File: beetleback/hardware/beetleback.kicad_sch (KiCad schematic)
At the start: 24 parts, among them J1 Conn_01x05_Female, J3 motor_pad_1, J4 motor_pad_2, Q1 IRF7351TRPBF, Q2 IRF7351TRPBF, U1 ATtiny13A-SS, U2 DRV8701P

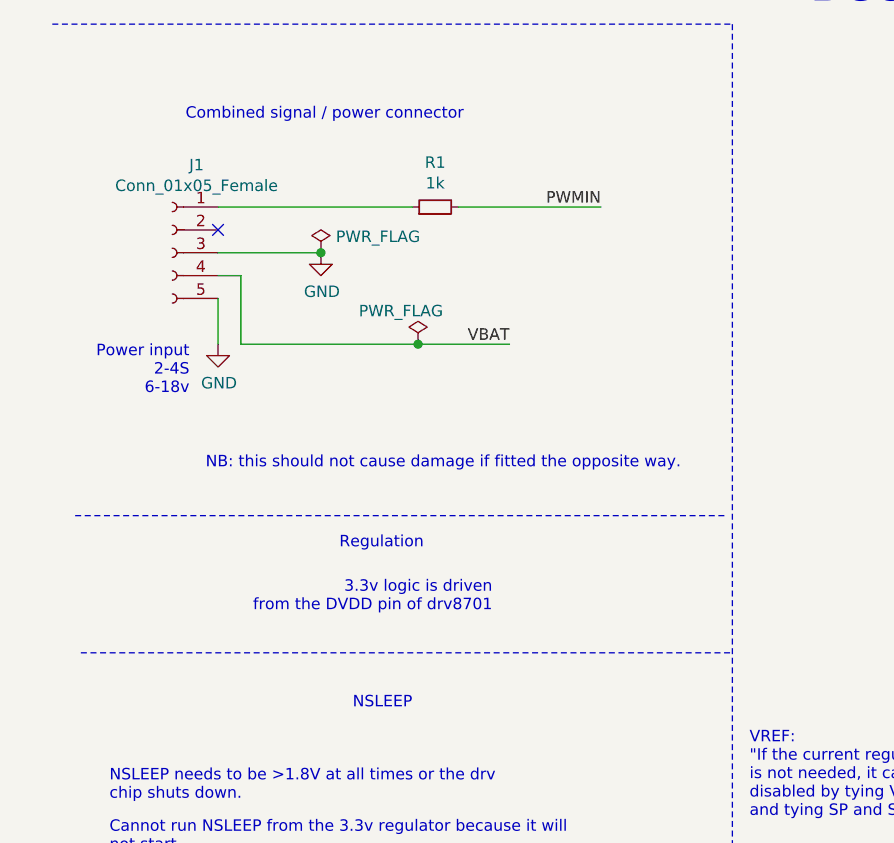
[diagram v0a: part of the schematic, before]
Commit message: Optional 5v regulator for RX
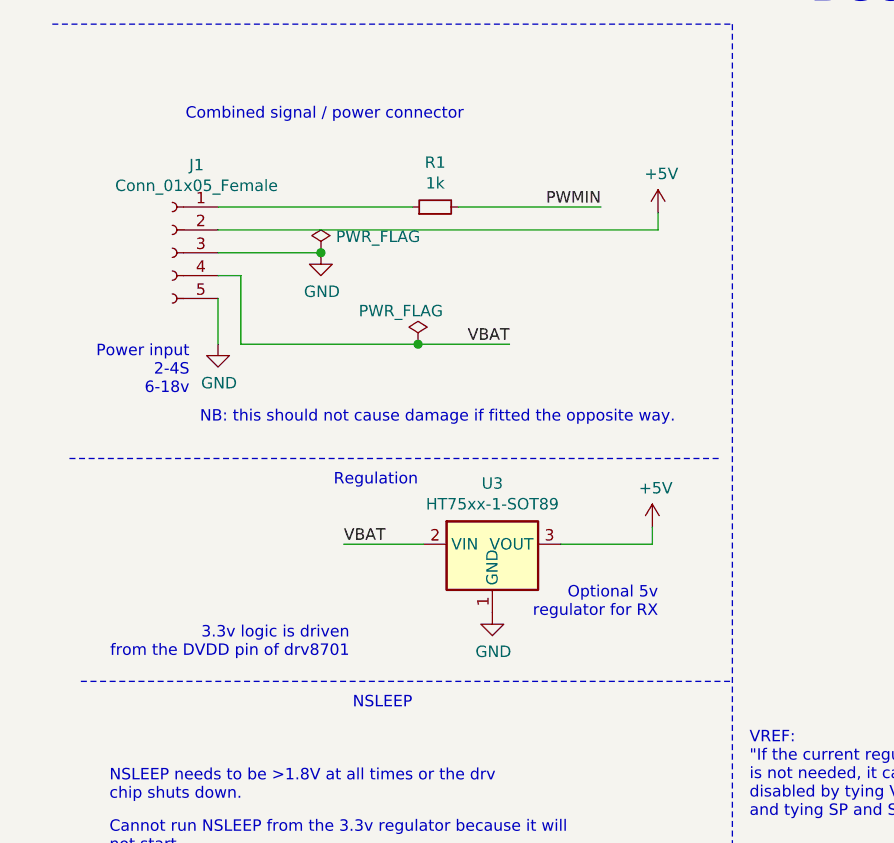
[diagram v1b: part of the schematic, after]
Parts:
- added U3: HT75xx-1-SOT89, Package_TO_SOT_SMD:SOT-89-3, symbol Regulator_Linear:HT75xx-1-SOT89
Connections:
- net GND: now also U3.1 (GND)
- net VBAT: now also U3.2 (VIN)
- net +5V: now reaches J1.2 (Pin_2)
- net +5V: now also U3.3 (VOUT)
- no-connect marks 4 -> 3
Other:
- note added: "Optional 5v regulator for RX"
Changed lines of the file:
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@@
   (junction (at 244.475 135.89) (diameter 1.016) (color 0 0 0 0))
   (junction (at 244.475 137.16) (diameter 1.016) (color 0 0 0 0))
-  (no_connect (at 27.94 50.8))
   (no_connect (at 178.435 66.04))
   (no_connect (at 182.88 118.745))
@@
     (stroke (width 0) (type solid) (color 0 0 0 0))
   )
+  (wire (pts (xy 27.94 50.8) (xy 76.835 50.8))
+    (stroke (width 0) (type solid) (color 0 0 0 0))
+  )
   (wire (pts (xy 27.94 53.34) (xy 39.37 53.34))
     (stroke (width 0) (type solid) (color 0 0 0 0))
@@
     (stroke (width 0) (type solid) (color 0 0 0 0))
   )
+  (wire (pts (xy 41.91 85.725) (xy 50.8 85.725))
+    (stroke (width 0) (type solid) (color 0 0 0 0))
+  )
   (wire (pts (xy 44.45 125.095) (xy 44.45 125.73))
     (stroke (width 0) (type solid) (color 0 0 0 0))
@@
     (stroke (width 0) (type solid) (color 0 0 0 0))
   )
+  (wire (pts (xy 66.04 85.725) (xy 76.2 85.725))
+    (stroke (width 0) (type solid) (color 0 0 0 0))
+  )
   (wire (pts (xy 67.945 170.18) (xy 76.835 170.18))
     (stroke (width 0) (type solid) (color 0 0 0 0))
@@
   )
   (wire (pts (xy 67.945 179.07) (xy 77.47 179.07))
+    (stroke (width 0) (type solid) (color 0 0 0 0))
+  )
+  (wire (pts (xy 76.2 83.82) (xy 76.2 85.725))
+    (stroke (width 0) (type solid) (color 0 0 0 0))
+  )
+  (wire (pts (xy 76.835 50.8) (xy 76.835 48.895))
     (stroke (width 0) (type solid) (color 0 0 0 0))
   )
@@
     (stroke (width 0) (type dash) (color 0 0 0 0))
   )
-  (polyline (pts (xy 12.065 82.55) (xy 84.455 82.55))
+  (polyline (pts (xy 11.43 76.2) (xy 83.82 76.2))
     (stroke (width 0) (type dash) (color 0 0 0 0))
   )
@@
     (stroke (width 0) (type dash) (color 0 0 0 0))
   )
-  (polyline (pts (xy 12.7 97.79) (xy 85.09 97.79))
+  (polyline (pts (xy 12.7 100.965) (xy 85.09 100.965))
     (stroke (width 0) (type dash) (color 0 0 0 0))
   )
@@
     (effects (font (size 1.27 1.27)) (justify right bottom))
   )
+  (text "3.3v logic is driven\nfrom the DVDD pin of drv8701" (at 42.545 98.425 180)
+    (effects (font (size 1.27 1.27)) (justify right bottom))
+  )
   (text "NSLEEP must not exceed 5.5V " (at 46.355 122.555 180)
     (effects (font (size 1.27 1.27)) (justify right bottom))
@@
     (effects (font (size 1.27 1.27)) (justify right bottom))
   )
-  (text "Regulation" (at 50.8 86.36 180)
+  (text "Regulation" (at 50.165 79.375 180)
     (effects (font (size 1.27 1.27)) (justify right bottom))
   )
@@
     (effects (font (size 1.27 1.27)) (justify right bottom))
   )
-  (text "3.3v logic is driven\nfrom the DVDD pin of drv8701" (at 58.42 93.345 180)
+  (text "Optional 5v\nregulator for RX" (at 76.835 93.98 180)
     (effects (font (size 1.27 1.27)) (justify right bottom))
   )
   (text "NB: this should not cause damage if fitted the opposite way."
-    (at 79.375 77.47 0)
+    (at 78.74 72.39 0)
     (effects (font (size 1.27 1.27)) (justify right bottom))
   )
@@
     (effects (font (size 1.27 1.27)) (justify left bottom))
   )
+  (label "VBAT" (at 41.91 85.725 0)
+    (effects (font (size 1.27 1.27)) (justify left bottom))
+  )
   (label "VBAT" (at 60.325 63.5 180)
     (effects (font (size 1.27 1.27)) (justify right bottom))
@@
     )
   )
+  (symbol (lib_id "power:+5V") (at 76.2 83.82 0) (unit 1)
+    (in_bom yes) (on_board yes)
+    (property "Reference" "#PWR017" (id 0) (at 76.2 87.63 0)
+      (effects (font (size 1.27 1.27)) hide)
+    )
+    (property "Value" "+5V" (id 1) (at 76.5683 79.4956 0))
+    (property "Footprint" "" (id 2) (at 76.2 83.82 0)
+      (effects (font (size 1.27 1.27)) hide)
+    )
+    (property "Datasheet" "" (id 3) (at 76.2 83.82 0)
+      (effects (font (size 1.27 1.27)) hide)
+    )
+  )
+  (symbol (lib_id "power:+5V") (at 76.835 48.895 0) (unit 1)
+    (in_bom yes) (on_board yes)
+    (property "Reference" "#PWR016" (id 0) (at 76.835 52.705 0)
+      (effects (font (size 1.27 1.27)) hide)
+    )
+    (property "Value" "+5V" (id 1) (at 77.2033 44.5706 0))
+    (property "Footprint" "" (id 2) (at 76.835 48.895 0)
+      (effects (font (size 1.27 1.27)) hide)
+    )
+    (property "Datasheet" "" (id 3) (at 76.835 48.895 0)
+      (effects (font (size 1.27 1.27)) hide)
+    )
+  )
   (symbol (lib_id "power:+3.3V") (at 163.195 42.545 0) (unit 1)
     (in_bom yes) (on_board yes)
@@
     )
     (property "Datasheet" "" (id 3) (at 39.37 144.145 0)
+      (effects (font (size 1.27 1.27)) hide)
+    )
+  )
+  (symbol (lib_id "power:GND") (at 58.42 93.345 0) (unit 1)
+    (in_bom yes) (on_board yes)
+    (property "Reference" "#PWR018" (id 0) (at 58.42 99.695 0)
+      (effects (font (size 1.27 1.27)) hide)
+    )
+    (property "Value" "GND" (id 1) (at 58.5343 97.6694 0))
+    (property "Footprint" "" (id 2) (at 58.42 93.345 0)
+      (effects (font (size 1.27 1.27)) hide)
+    )
+    (property "Datasheet" "" (id 3) (at 58.42 93.345 0)
       (effects (font (size 1.27 1.27)) hide)
     )
@@
     )
   )
+  (symbol (lib_id "Regulator_Linear:HT75xx-1-SOT89") (at 58.42 88.265 0) (unit 1)
+    (in_bom yes) (on_board yes)
+    (property "Reference" "U3" (id 0) (at 58.42 78.9748 0))
+    (property "Value" "HT75xx-1-SOT89" (id 1) (at 58.42 81.2735 0))
+    (property "Footprint" "Package_TO_SOT_SMD:SOT-89-3" (id 2) (at 58.42 80.01 0)
+      (effects (font (size 1.27 1.27) italic) hide)
+    )
+    (property "Datasheet" "https://www.holtek.com/documents/10179/116711/HT75xx-1v250.pdf" (id 3) (at 58.42 85.725 0)
+      (effects (font (size 1.27 1.27)) hide)
+    )
+  )
   (symbol (lib_id "MCU_Microchip_ATtiny:ATtiny13A-SS") (at 163.195 60.96 0) (unit 1)
     (in_bom yes) (on_board yes)
@@
       (reference "#PWR015") (unit 1) (value "GND") (footprint "")
     )
+    (path "/3626eb41-deee-4521-ae53-d8eee93f730a"
+      (reference "#PWR016") (unit 1) (value "+5V") (footprint "")
+    )
+    (path "/f5ba5b88-6463-4bc7-985a-2101176f5a3b"
+      (reference "#PWR017") (unit 1) (value "+5V") (footprint "")
+    )
+    (path "/18b2d887-f7d1-42e4-aea1-010d6749f2ab"
+      (reference "#PWR018") (unit 1) (value "GND") (footprint "")
+    )
     (path "/975884ae-c191-4f7a-ae32-6dd10ac01641"
       (reference "#PWR0102") (unit 1) (value "GND") (footprint "")
@@
       (reference "U2") (unit 1) (value "DRV8701P") (footprint "Package_DFN_QFN:VQFN-24-1EP_4x4mm_P0.5mm_EP2.45x2.45mm")
     )
-  )
+    (path "/c57027af-d7b7-4cbc-ba3b-142dfb36a1aa"
+      (reference "U3") (unit 1) (value "HT75xx-1-SOT89") (footprint "Package_TO_SOT_SMD:SOT-89-3")
+    )
+  )

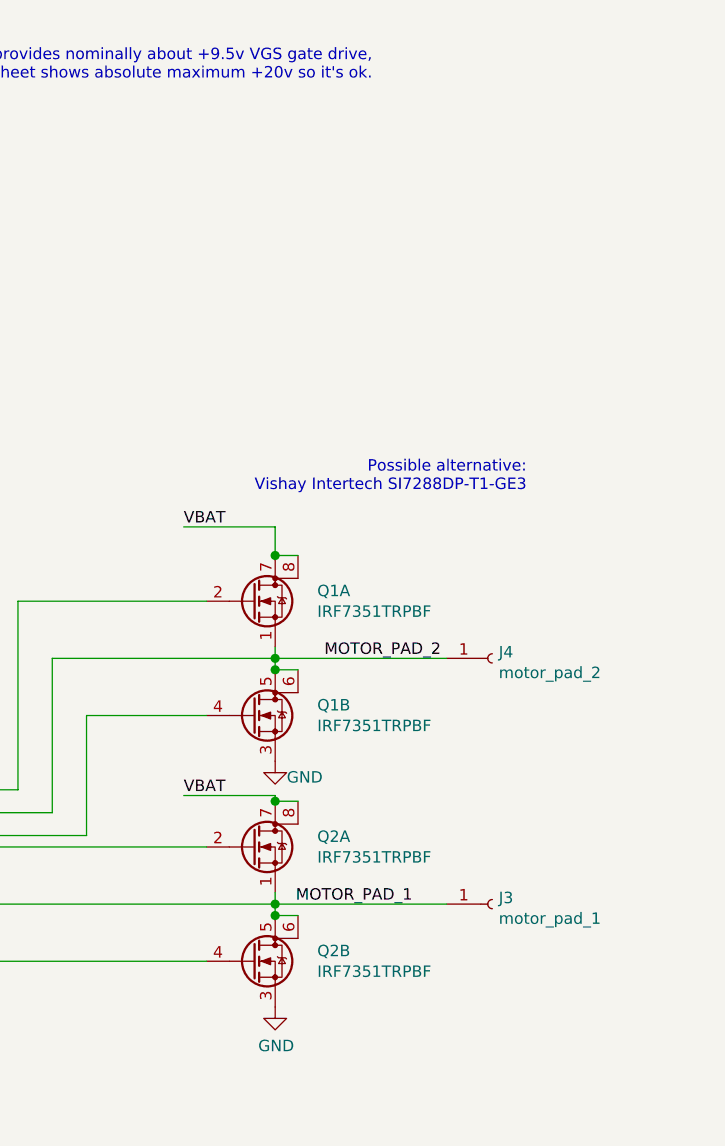
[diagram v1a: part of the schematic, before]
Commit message: Rev2 hardware: update mosfet, silkscreen tweaks, lcsc part numbers
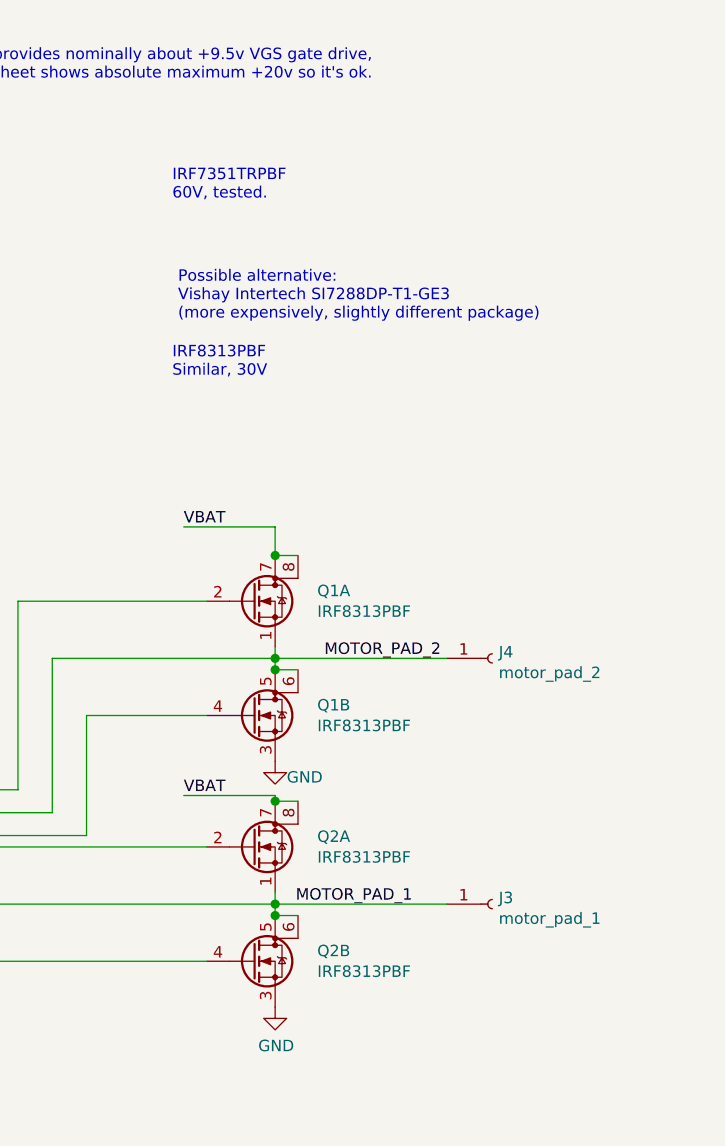
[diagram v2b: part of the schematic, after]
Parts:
- Q1, Q2: value IRF7351TRPBF -> IRF8313PBF; LCSC C68403 -> C57696
- R5: LCSC (none) -> C25879
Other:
- note added: "IRF7351TRPBF 60V, tested."
- note added: "IRF8313PBF Similar, 30V"
- note added: "Possible alternative: Vishay Intertech SI7288DP-T1-GE3 (more expensively, slightly different package)"
- note removed: "Possible alternative: Vishay Intertech SI7288DP-T1-GE3"
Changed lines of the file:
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@@
+    (effects (font (size 1.27 1.27)) (justify left bottom))
+  )
+  (text "IRF7351TRPBF\n60V, tested. " (at 233.045 57.785 0)
+    (effects (font (size 1.27 1.27)) (justify left bottom))
+  )
+  (text "IRF8313PBF\nSimilar, 30V " (at 233.045 77.47 0)
+    (effects (font (size 1.27 1.27)) (justify left bottom))
+  )
+  (text "Possible alternative:\nVishay Intertech SI7288DP-T1-GE3 \n(more expensively, slightly different package)"
+    (at 233.68 71.12 0)
     (effects (font (size 1.27 1.27)) (justify left bottom))
   )
   (text "drv8701 provides nominally about +9.5v VGS gate drive,\nmosfets datasheet shows absolute maximum +20v so it's ok."
     (at 255.27 44.45 0)
-    (effects (font (size 1.27 1.27)) (justify right bottom))
-  )
-  (text "Possible alternative:\nVishay Intertech SI7288DP-T1-GE3 "
-    (at 272.415 90.17 0)
     (effects (font (size 1.27 1.27)) (justify right bottom))
   )
@@
       (effects (font (size 1.27 1.27)) hide)
     )
-    (property "LCSC" "" (id 4) (at 44.45 129.54 0)
+    (property "LCSC" "C25879" (id 4) (at 44.45 129.54 0)
       (effects (font (size 1.27 1.27)) hide)
     )
@@
       (effects (font (size 1.27 1.27)) (justify left))
     )
-    (property "Value" "IRF7351TRPBF" (id 1) (at 249.149 103.384 0)
+    (property "Value" "IRF8313PBF" (id 1) (at 249.149 103.384 0)
       (effects (font (size 1.27 1.27)) (justify left))
     )
@@
       (effects (font (size 1.27 1.27)) hide)
     )
-    (property "LCSC" "C68403" (id 4) (at 241.935 102.235 0)
+    (property "LCSC" "C57696" (id 4) (at 241.935 102.235 0)
       (effects (font (size 1.27 1.27)) hide)
     )
@@
       (effects (font (size 1.27 1.27)) (justify left))
     )
-    (property "Value" "IRF7351TRPBF" (id 1) (at 249.149 116.084 0)
+    (property "Value" "IRF8313PBF" (id 1) (at 249.149 116.084 0)
       (effects (font (size 1.27 1.27)) (justify left))
     )
@@
       (effects (font (size 1.27 1.27)) hide)
     )
-    (property "LCSC" "C68403" (id 4) (at 241.935 114.935 0)
+    (property "LCSC" "C57696" (id 4) (at 241.935 114.935 0)
       (effects (font (size 1.27 1.27)) hide)
     )
@@
       (effects (font (size 1.27 1.27)) (justify left))
     )
-    (property "Value" "IRF7351TRPBF" (id 1) (at 249.149 130.689 0)
+    (property "Value" "IRF8313PBF" (id 1) (at 249.149 130.689 0)
       (effects (font (size 1.27 1.27)) (justify left))
     )
@@
       (effects (font (size 1.27 1.27)) hide)
     )
-    (property "LCSC" "C68403" (id 4) (at 241.935 129.54 0)
+    (property "LCSC" "C57696" (id 4) (at 241.935 129.54 0)
       (effects (font (size 1.27 1.27)) hide)
     )
@@
       (effects (font (size 1.27 1.27)) (justify left))
     )
-    (property "Value" "IRF7351TRPBF" (id 1) (at 249.149 143.389 0)
+    (property "Value" "IRF8313PBF" (id 1) (at 249.149 143.389 0)
       (effects (font (size 1.27 1.27)) (justify left))
     )
@@
       (effects (font (size 1.27 1.27)) hide)
     )
-    (property "LCSC" "C68403" (id 4) (at 241.935 142.24 0)
+    (property "LCSC" "C57696" (id 4) (at 241.935 142.24 0)
       (effects (font (size 1.27 1.27)) hide)
     )
@@
     )
     (path "/a69a273c-4e3e-46dc-8062-8d9f361d07d3"
-      (reference "Q1") (unit 1) (value "IRF7351TRPBF") (footprint "Package_SO:SOIC-8_3.9x4.9mm_P1.27mm")
+      (reference "Q1") (unit 1) (value "IRF8313PBF") (footprint "Package_SO:SOIC-8_3.9x4.9mm_P1.27mm")
     )
     (path "/86cb0b69-ddbd-42cc-8e88-2d4ebc15451c"
-      (reference "Q1") (unit 2) (value "IRF7351TRPBF") (footprint "Package_SO:SOIC-8_3.9x4.9mm_P1.27mm")
+      (reference "Q1") (unit 2) (value "IRF8313PBF") (footprint "Package_SO:SOIC-8_3.9x4.9mm_P1.27mm")
     )
     (path "/d094f7e5-7051-4491-9470-d138e254b828"
-      (reference "Q2") (unit 1) (value "IRF7351TRPBF") (footprint "Package_SO:SOIC-8_3.9x4.9mm_P1.27mm")
+      (reference "Q2") (unit 1) (value "IRF8313PBF") (footprint "Package_SO:SOIC-8_3.9x4.9mm_P1.27mm")
     )
     (path "/fdf323e3-1e06-45a9-b347-9010497d9e39"
-      (reference "Q2") (unit 2) (value "IRF7351TRPBF") (footprint "Package_SO:SOIC-8_3.9x4.9mm_P1.27mm")
+      (reference "Q2") (unit 2) (value "IRF8313PBF") (footprint "Package_SO:SOIC-8_3.9x4.9mm_P1.27mm")
     )
     (path "/66241c81-47d1-4787-abff-1a86cfe19362"
